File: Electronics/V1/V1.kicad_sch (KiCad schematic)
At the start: 13 parts, among them U1 ADPD144RI, U2 TCA9517ADGK, U3 XIAO-ESP32-C3, U4 TPS72218

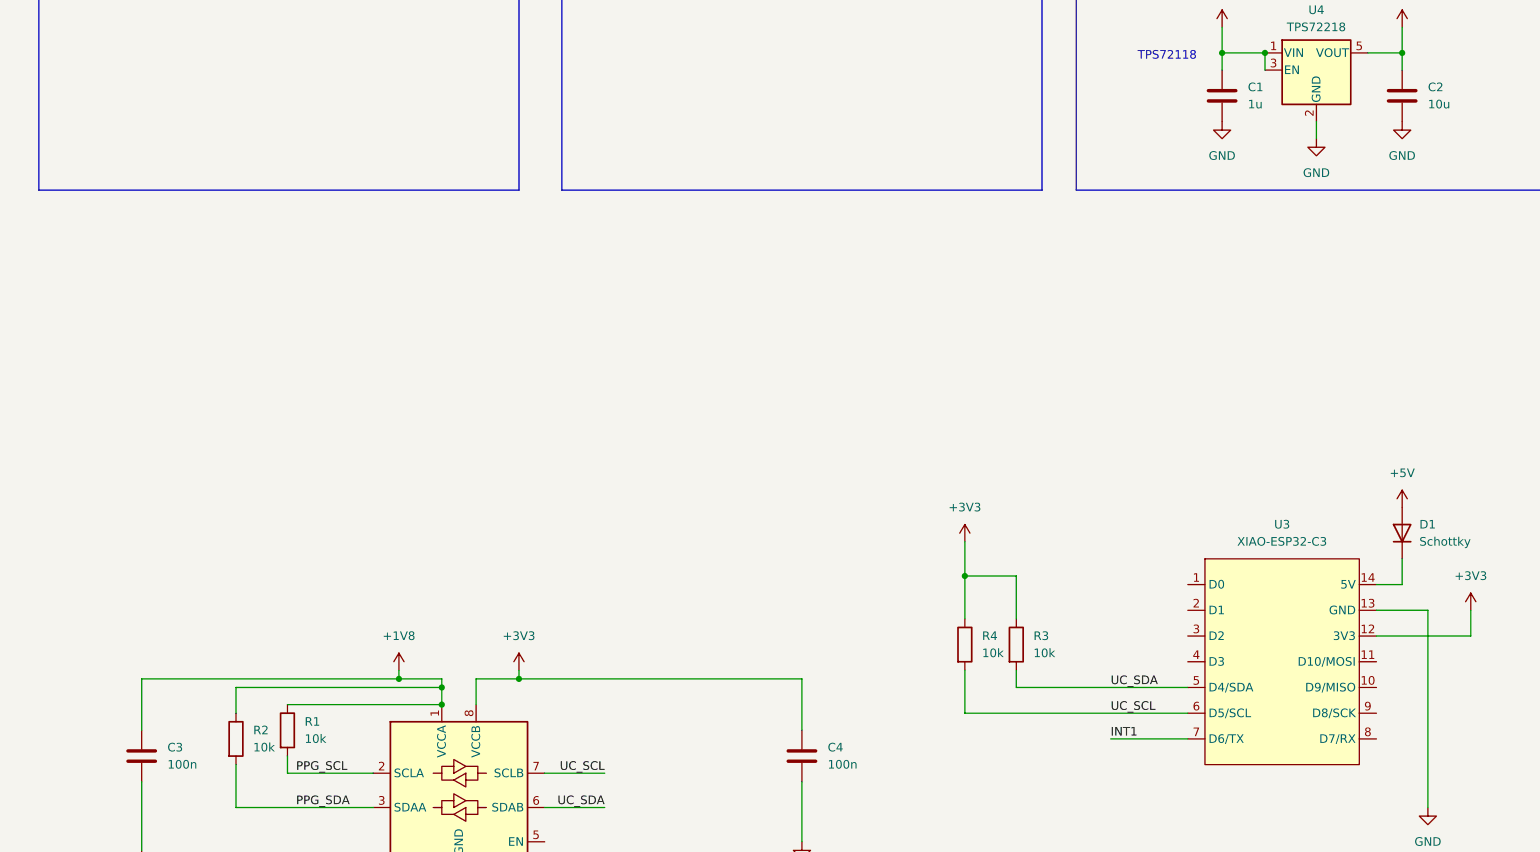
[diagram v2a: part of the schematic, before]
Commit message: Added footprint for ADPD144
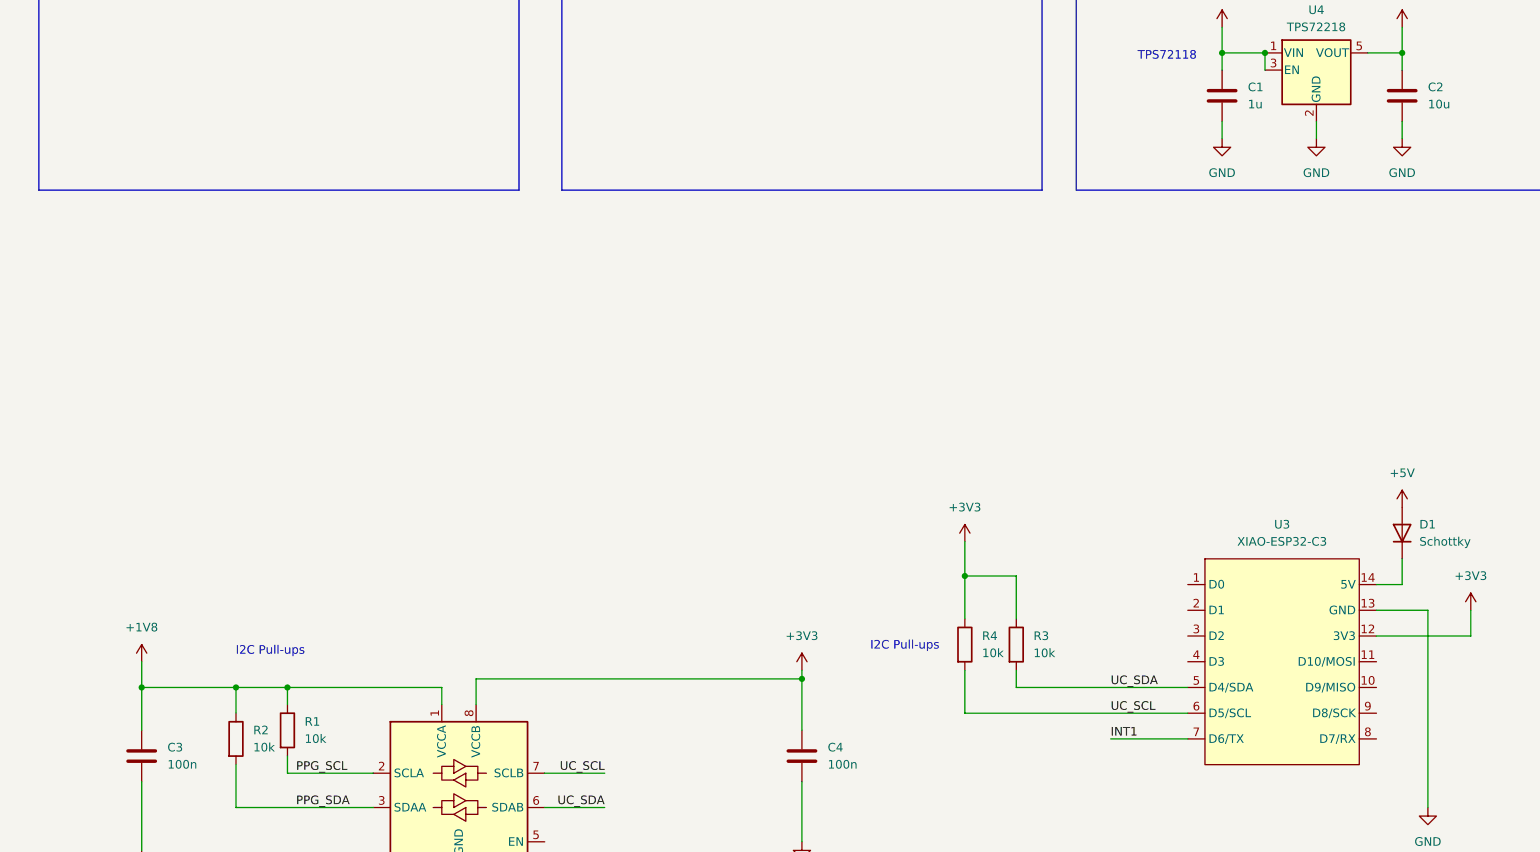
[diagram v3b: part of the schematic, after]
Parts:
- U1: footprint (none) -> CUSTOM:CE-12-2
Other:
- note added: "I2C Pull-ups"
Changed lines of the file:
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@@
+		)
+	)
+	(text "I2C Pull-ups"
+		(exclude_from_sim no)
+		(at 147.32 122.174 0)
+		(effects
+			(font
+				(size 1.27 1.27)
+			)
 		)
 	)
@@
 		)
 	)
-	(junction
-		(at 72.39 127)
-		(diameter 0)
-		(color 0 0 0 0)
-	)
-	(junction
-		(at 78.74 130.81)
-		(diameter 0)
-		(color 0 0 0 0)
+	(text "I2C Pull-ups"
+		(exclude_from_sim no)
+		(at 53.34 122.936 0)
+		(effects
+			(font
+				(size 1.27 1.27)
+			)
+		)
 	)
 	(junction
@@
 	)
 	(junction
-		(at 90.17 127)
+		(at 34.29 128.27)
 		(diameter 0)
 		(color 0 0 0 0)
 	)
 	(junction
-		(at 78.74 128.27)
+		(at 48.26 128.27)
 		(diameter 0)
 		(color 0 0 0 0)
 	)
+	(junction
+		(at 55.88 128.27)
+		(diameter 0)
+		(color 0 0 0 0)
+	)
+	(junction
+		(at 132.08 127)
+		(diameter 0)
+		(color 0 0 0 0)
+	)
 	(no_connect
 		(at 11.43 74.93)
@@
 	(wire
 		(pts
-			(xy 90.17 127) (xy 132.08 127)
-		)
-		(stroke
-			(width 0)
-			(type default)
-		)
-	)
-	(wire
-		(pts
 			(xy 194.31 34.29) (xy 200.66 34.29)
 		)
@@
 	(wire
 		(pts
+			(xy 194.31 46.99) (xy 194.31 44.45)
+		)
+		(stroke
+			(width 0)
+			(type default)
+		)
+	)
+	(wire
+		(pts
 			(xy 224.79 116.84) (xy 217.17 116.84)
 		)
@@
 	(wire
 		(pts
-			(xy 48.26 128.27) (xy 78.74 128.27)
+			(xy 48.26 128.27) (xy 55.88 128.27)
 		)
 		(stroke
@@
 	(wire
 		(pts
-			(xy 72.39 127) (xy 78.74 127)
-		)
-		(stroke
-			(width 0)
-			(type default)
-		)
-	)
-	(wire
-		(pts
 			(xy 194.31 34.29) (xy 194.31 36.83)
 		)
@@
 	(wire
 		(pts
-			(xy 72.39 125.73) (xy 72.39 127)
+			(xy 220.98 46.99) (xy 220.98 44.45)
 		)
 		(stroke
@@
 	(wire
 		(pts
+			(xy 55.88 128.27) (xy 55.88 130.81)
+		)
+		(stroke
+			(width 0)
+			(type default)
+		)
+	)
+	(wire
+		(pts
 			(xy 224.79 146.05) (xy 224.79 116.84)
 		)
@@
 	(wire
 		(pts
-			(xy 90.17 125.73) (xy 90.17 127)
+			(xy 132.08 125.73) (xy 132.08 127)
 		)
 		(stroke
@@
 	(wire
 		(pts
-			(xy 55.88 130.81) (xy 78.74 130.81)
+			(xy 55.88 128.27) (xy 78.74 128.27)
 		)
 		(stroke
@@
 	(wire
 		(pts
-			(xy 78.74 127) (xy 78.74 128.27)
-		)
-		(stroke
-			(width 0)
-			(type default)
-		)
-	)
-	(wire
-		(pts
-			(xy 34.29 134.62) (xy 34.29 127)
+			(xy 34.29 134.62) (xy 34.29 128.27)
 		)
 		(stroke
@@
 	(wire
 		(pts
-			(xy 34.29 127) (xy 72.39 127)
-		)
-		(stroke
-			(width 0)
-			(type default)
-		)
-	)
-	(wire
-		(pts
-			(xy 83.82 127) (xy 90.17 127)
+			(xy 34.29 128.27) (xy 48.26 128.27)
+		)
+		(stroke
+			(width 0)
+			(type default)
+		)
+	)
+	(wire
+		(pts
+			(xy 83.82 127) (xy 132.08 127)
 		)
 		(stroke
@@
 		(pts
 			(xy 231.14 120.65) (xy 217.17 120.65)
+		)
+		(stroke
+			(width 0)
+			(type default)
+		)
+	)
+	(wire
+		(pts
+			(xy 34.29 124.46) (xy 34.29 128.27)
 		)
 		(stroke
@@
 	(symbol
 		(lib_id "power:GND")
-		(at 220.98 44.45 0)
+		(at 220.98 46.99 0)
 		(unit 1)
 		(exclude_from_sim no)
@@
 		(fields_autoplaced yes)
 		(property "Reference" "#PWR012"
-			(at 220.98 50.8 0)
+			(at 220.98 53.34 0)
 			(effects
 				(font
@@
 		)
 		(property "Value" "GND"
-			(at 220.98 49.53 0)
+			(at 220.98 52.07 0)
 			(effects
 				(font
@@
 		)
 		(property "Footprint" ""
-			(at 220.98 44.45 0)
+			(at 220.98 46.99 0)
 			(effects
 				(font
@@
 		)
 		(property "Datasheet" ""
-			(at 220.98 44.45 0)
+			(at 220.98 46.99 0)
 			(effects
 				(font
@@
 		)
 		(property "Description" "Power symbol creates a global label with name \"GND\" , ground"
-			(at 220.98 44.45 0)
+			(at 220.98 46.99 0)
 			(effects
 				(font
@@
 	(symbol
 		(lib_id "power:+1V8")
-		(at 72.39 125.73 0)
+		(at 34.29 124.46 0)
 		(unit 1)
 		(exclude_from_sim no)
@@
 		(fields_autoplaced yes)
 		(property "Reference" "#PWR07"
-			(at 72.39 129.54 0)
+			(at 34.29 128.27 0)
 			(effects
 				(font
@@
 		)
 		(property "Value" "+1V8"
-			(at 72.39 120.65 0)
+			(at 34.29 119.38 0)
 			(effects
 				(font
@@
 		)
 		(property "Footprint" ""
-			(at 72.39 125.73 0)
+			(at 34.29 124.46 0)
 			(effects
 				(font
@@
 		)
 		(property "Datasheet" ""
-			(at 72.39 125.73 0)
+			(at 34.29 124.46 0)
 			(effects
 				(font
@@
 		)
 		(property "Description" "Power symbol creates a global label with name \"+1V8\""
-			(at 72.39 125.73 0)
+			(at 34.29 124.46 0)
 			(effects
 				(font
@@
 			)
 		)
-		(property "Footprint" ""
+		(property "Footprint" "CUSTOM:CE-12-2"
 			(at 81.28 213.36 0)
 			(effects
@@
 	(symbol
 		(lib_id "power:GND")
-		(at 194.31 44.45 0)
+		(at 194.31 46.99 0)
 		(unit 1)
 		(exclude_from_sim no)
@@
 		(fields_autoplaced yes)
 		(property "Reference" "#PWR011"
-			(at 194.31 50.8 0)
+			(at 194.31 53.34 0)
 			(effects
 				(font
@@
 		)
 		(property "Value" "GND"
-			(at 194.31 49.53 0)
+			(at 194.31 52.07 0)
 			(effects
 				(font
@@
 		)
 		(property "Footprint" ""
-			(at 194.31 44.45 0)
+			(at 194.31 46.99 0)
 			(effects
 				(font
@@
 		)
 		(property "Datasheet" ""
-			(at 194.31 44.45 0)
+			(at 194.31 46.99 0)
 			(effects
 				(font
@@
 		)
 		(property "Description" "Power symbol creates a global label with name \"GND\" , ground"
-			(at 194.31 44.45 0)
+			(at 194.31 46.99 0)
 			(effects
 				(font
@@
 	(symbol
 		(lib_id "power:+3V3")
-		(at 90.17 125.73 0)
+		(at 132.08 125.73 0)
 		(unit 1)
 		(exclude_from_sim no)
@@
 		(fields_autoplaced yes)
 		(property "Reference" "#PWR09"
-			(at 90.17 129.54 0)
+			(at 132.08 129.54 0)
 			(effects
 				(font
@@
 		)
 		(property "Value" "+3V3"
-			(at 90.17 120.65 0)
+			(at 132.08 120.65 0)
 			(effects
 				(font
@@
 		)
 		(property "Footprint" ""
-			(at 90.17 125.73 0)
+			(at 132.08 125.73 0)
 			(effects
 				(font
@@
 		)
 		(property "Datasheet" ""
-			(at 90.17 125.73 0)
+			(at 132.08 125.73 0)
 			(effects
 				(font
@@
 		)
 		(property "Description" "Power symbol creates a global label with name \"+3V3\""
-			(at 90.17 125.73 0)
-			(effects
-				(font
+			(at 132.08 125.73 0)
+			(effects
+				(font

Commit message: Added more symbols and footprints
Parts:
- added C5: 100n, Capacitor_SMD:C_0805_2012Metric_Pad1.18x1.45mm_HandSolder, symbol Device:C
- added C6: 100n, Capacitor_SMD:C_0603_1608Metric_Pad1.08x0.95mm_HandSolder, symbol Device:C
- added C7: 4u7, Capacitor_SMD:C_0603_1608Metric_Pad1.08x0.95mm_HandSolder, symbol Device:C
- added C8: 1u, Capacitor_SMD:C_0603_1608Metric_Pad1.08x0.95mm_HandSolder, symbol Device:C
- added LED1, LED2, LED3: ~, symbol Device:LED
- added PD1, PD2, PD3, PD4: D_Photo, CUSTOM:SFH2704 Photodiode, symbol Device:D_Photo
- added U5: ADPD1080, Package_CSP:LFCSP-28-1EP_5x5mm_P0.5mm_EP3.14x3.14mm, symbol CUSTOM:ADPD1080 Analog Front End
- added U6: LP2989 LDO Regulator, Package_SO:SOIC-8_3.9x4.9mm_P1.27mm, symbol CUSTOM:LP2989 LDO Regulator
- C3, C4: footprint Capacitor_SMD:C_0603_1608Metric_Pad1.08x0.95mm_HandSolder -> Capacitor_SMD:C_0805_2012Metric_Pad1.18x1.45mm_HandSolder
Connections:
- net +1V8: now also C5.1, C6.1, U5.3 (DVDD), U5.6 (AVDD)
- net GND: now also C5.2, C6.2, C7.2, C8.2, U5.26 (LGND), U5.29 (DGND), U5.4 (AGND)
- net PPG_SCL: now also U5.27 (SCL)
- net PPG_SDA: now also U5.28 (SDA)
- new net: PD4.2 (A), U5.10 (PD4)
- new net: PD3.2 (A), U5.9 (PD3)
- new net: LED1.1 (K), U5.23 (LEDX1)
- new net: LED3.1 (K), U5.25 (LEDX3)
- new net: PD2.2 (A), U5.8 (PD2)
- new net: C8.1, U5.5 (VREF)
- new net: U5.16 (NC), U5.17 (NC), U5.18 (NC), U5.19 (NC), U5.20 (NC), U5.21 (NC), U5.22 (NC)
- new net: LED2.1 (K), U5.24 (LEDX2)
- new net: PD1.2 (A), U5.7 (PD1)
- new net AFE_0: U5.1 (GPIO0)
- new net AFE_1: U5.2 (GPIO1)
- new net PD_K: PD1.1 (K), PD2.1 (K), PD3.1 (K), PD4.1 (K), U5.11 (PDC)
- new net VLED: C7.1, LED1.2 (A), LED2.2 (A), LED3.2 (A)
- no-connect marks 1 -> 5
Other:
- note added: "1.8V Reg"
- note added: "3.3V Reg"
- note added: "3.3V for VLED (N.B. Microcontroller does not put out enough current for LED) Current minimum: 500mA"
- note added: "3V - 9V"
- note added: "5V Supply for Microcontroller (N.B. use 5V as main VCC bus) 500mA ish. Vin = 3-9V ish"
- note added: "5V supply"
- note added: "Battery"
- note added: "Microcontroller"
- note removed: "3.3V for VLED (N.B. Microcontroller does not put out enough current for LED)"
- note removed: "5V Supply for Microcontroller (N.B. use 5V as main VCC bus)"
- moved on the sheet: C4

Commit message: Added level shifter for gpio, 5V reg, battery monitor and changed some footprints.
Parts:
- removed LED1, LED2, LED3: ~, symbol Device:LED
- removed U1: ADPD144RI, CUSTOM:CE-12-2, symbol CUSTOM:ADPD144RI
- added C10, C9: 100n, Capacitor_SMD:C_0805_2012Metric_Pad1.18x1.45mm_HandSolder, symbol Device:C
- added C11, C12: 10uF, symbol Device:C_Polarized
- added D2: Schottky, symbol Device:D
- added D3, D4: 3V3 LED, symbol Device:LED
- added J1: BATTERY, symbol Connector_Generic:Conn_01x02
- added J3: GPIO, Connector_PinHeader_2.54mm:PinHeader_1x08_P2.54mm_Vertical, symbol Connector_Generic:Conn_01x08
- added LED1: SFH-7016, CUSTOM:SFH-7016 Multi Chip LED, symbol CUSTOM:SFH-7016
- added R10, R9: 330, symbol Device:R
- added R5: changeme, symbol Device:R
- added R6: 0R, symbol Device:R
- added R7: 15k, symbol Device:R
- added R8: 12k, symbol Device:R
- added SW1: SW_SPST, symbol Switch:SW_SPST
- added U7: TXB0102DCU, Package_SO:VSSOP-8_2.3x2mm_P0.5mm, symbol Logic_LevelTranslator:TXB0102DCU
- added U8: MAX603, Package_DIP:DIP-8_W10.16mm_LongPads, symbol Regulator_Linear:MAX603
- PD1, PD2, PD3, PD4: value D_Photo -> SFH2200; footprint CUSTOM:SFH2704 Photodiode -> CUSTOM:TOPLED D5140
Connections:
- net +1V8: now also C9.1, R6.1, U7.3 (VCCA)
- net +3V3: now also C10.1, J3.3 (Pin_3), R9.1, U7.7 (VCCB)
- net +5V: now also C12.1, J3.1 (Pin_1), U8.8 (OUT)
- net AFE_0: now also U7.5 (A1)
- net AFE_1: now also U7.4 (A2)
- net GND: now also C10.2, C11.2, C12.2, C9.2, D3.1 (K), D4.1 (K), J3.2 (Pin_2), J3.4 (Pin_4), R5.2, R8.2, SW1.2 (B), U7.2 (GND), U8.2 (GND), U8.3 (GND), U8.5 (SET), U8.6 (GND), U8.7 (GND)
- net VLED: now also LED1.2 (A), LED1.2 (A), LED1.2 (A), LED1.5 (A), LED1.5 (A), LED1.5 (A)
- net at U5.23 (LEDX1): now also LED1.1 (KIR)
- net at U5.25 (LEDX3): now also LED1.4 (KRED)
- net at U5.24 (LEDX2): now also LED1.3 (KGREEN)
- net UC_D0: now reaches U3.1 (D0)
- net UC_D0: now also U7.8 (B1)
- net UC_D9: now reaches U3.10 (D9/MISO)
- net UC_D9: now also J3.6 (Pin_6)
- net UC_D10: now reaches U3.11 (D10/MOSI)
- net UC_D10: now also J3.5 (Pin_5)
- net UC_D1: now reaches U3.2 (D1)
- net UC_D1: now also U7.1 (B2)
- net BAT_SENSE: now reaches U3.3 (D2)
- net BAT_SENSE: now also R7.2, R8.1
- net I2C_EN: now reaches U3.4 (D3)
- net I2C_EN: now also U2.5 (EN)
- net UC_D7: now reaches U3.8 (D7/RX)
- net UC_D7: now also J3.8 (Pin_8)
- net UC_D8: now reaches U3.9 (D8/SCK)
- net UC_D8: now also J3.7 (Pin_7)
- net INT1 renamed UC_D6
- net UC_D6: now also R10.1
- new net: D4.2 (A), R10.2
- new net: R5.1, R6.2, U7.6 (OE)
- new net: D3.2 (A), R9.2
- new net BAT+: D2.2 (A), J1.1 (Pin_1)
- new net BAT-: J1.2 (Pin_2), SW1.1 (A)
- new net VBAT: C11.1, D2.1 (K), R7.1, U8.1 (IN), U8.4 (~{OFF})
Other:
- note added: "0.45 Voltage divider for battery voltage sensing."
- note added: "Choose a pull down"
- note added: "Define VLED"
- note added: "Do i need this?"
- note added: "Green"
- note added: "Infrared"
- note added: "Red"
- note added: "Verfiy pins"
- note added: "gpio Level shifter required for communication between OFE (1.8V) and Microcontroller (3.3v)"
- note added: "i2c Level shifter required for communication between OFE (1.8V) and Microcontroller (3.3v)"
- note removed: "Level shifter required for communication between OFE (1.8V) and Microcontroller (3.3v)"
- note removed: "TODO: Add I2C pull-up resistors"
- moved on the sheet: C1, C2, C3, C4, C5, C6, C7, C8, PD1, R1, R2, U2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

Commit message: Added Seeed Studio footprint
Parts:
- removed U6: LP2989 LDO Regulator, Package_SO:SOIC-8_3.9x4.9mm_P1.27mm, symbol CUSTOM:LP2989 LDO Regulator
- C10, C3, C4, C5, C9: footprint Capacitor_SMD:C_0805_2012Metric_Pad1.18x1.45mm_HandSolder -> Capacitor_SMD:C_0603_1608Metric_Pad1.08x0.95mm_HandSolder
- C11, C12: footprint (none) -> Capacitor_SMD:C_1210_3225Metric_Pad1.33x2.70mm_HandSolder
- D1, D2: value Schottky -> B130LAW-7-F; footprint (none) -> Diode_SMD:D_SOD-123
- D3, D4: footprint (none) -> LED_SMD:LED_0805_2012Metric_Pad1.15x1.40mm_HandSolder
- J1: footprint (none) -> TerminalBlock:TerminalBlock_bornier-2_P5.08mm
- R1, R10, R2, R3, R4, R5, R6, R7, R8, R9: footprint (none) -> Resistor_SMD:R_0603_1608Metric_Pad0.98x0.95mm_HandSolder
- U3: footprint (none) -> CUSTOM:Seeed Studio XIAO ESP32-C3
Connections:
- no-connect marks 5 -> 4
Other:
- note removed: "1.8V Reg"
- note removed: "3.3V Reg"
- note removed: "3V - 9V"
- note removed: "5V supply"
- note removed: "Battery"
- note removed: "Microcontroller"
- moved on the sheet: D2, D3, J1, R7, R8, R9, SW1

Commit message: Minor fixes
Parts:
- D4: value 3V3 LED -> CTRL LED
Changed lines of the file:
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@@
 			)
 		)
-		(property "Value" "3V3 LED"
+		(property "Value" "CTRL LED"
 			(at 181.61 155.2574 90)
 			(effects

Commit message: Some unfinished PCB changes
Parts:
- removed D2: B130LAW-7-F, Diode_SMD:D_SOD-123, symbol Device:D
- removed SW1: SW_SPST, symbol Switch:SW_SPST
- removed U8: MAX603, Package_DIP:DIP-8_W10.16mm_LongPads, symbol Regulator_Linear:MAX603
- added H1, H2: MountingHole, MountingHole:MountingHole_3.2mm_M3, symbol Mechanical:MountingHole
- added Q1, Q3: PMV41XPAR, Package_TO_SOT_SMD:SOT-23, symbol Transistor_FET:AO3401A
- added R11: 10k, Resistor_SMD:R_0603_1608Metric_Pad0.98x0.95mm_HandSolder, symbol Device:R
- added R12: 0R, Resistor_SMD:R_0603_1608Metric_Pad0.98x0.95mm_HandSolder, symbol Device:R
- added SW1: PVA1 EE H1 3.5N V2, Button_Switch_THT:SW_Push_2P1T_Toggle_CK_PVA1xxH1xxxxxxV2, symbol Switch:SW_DPST
- added U1: TPS7A4533, Package_TO_SOT_SMD:SOT-223-6, symbol CUSTOM:TPS7A45xx
- C11, C12: footprint Capacitor_SMD:C_1210_3225Metric_Pad1.33x2.70mm_HandSolder -> Capacitor_SMD:C_0805_2012Metric_Pad1.18x1.45mm_HandSolder
- J1: value BATTERY -> BA9VPC; footprint TerminalBlock:TerminalBlock_bornier-2_P5.08mm -> Battery:BatteryHolder_MPD_BA9VPC_1xPP3
- R7: value 15k -> 20k
- R8: value 12k -> 10k
- U3: symbol CUSTOM:Seeed_XIAO_ESP32 -> CUSTOM:Seeed_XIAO_ESP32 Development Board
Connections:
- net BAT- is gone; now on net GND: J1.2 (Pin_2)
- net VLED is gone; now on net +3V3: C7.1, LED1.2 (A), LED1.2 (A), LED1.2 (A), LED1.5 (A), LED1.5 (A), LED1.5 (A)
- net +3V3: now also C1.1, C12.1, J3.1 (Pin_1), J3.2 (Pin_2), U4.1 (VIN), U4.3 (EN), Q1.3 (D), U1.4 (OUT), U1.5 (ADJ); no longer J3.3 (Pin_3), R9.1, U3.12 (3V3)
- net BAT+: now also Q3.3 (D), R11.1, R12.1
- net GND: now also J3.3 (Pin_3), SW1.2, SW1.4, U1.3 (GND), U1.6 (GND); no longer J3.2 (Pin_2)
- net VBAT: now also D1.1 (K), U1.1 (~{SHDN}), U1.2 (IN)
- net VUSB: now reaches U3.14 (5V)
- net VUSB: now also Q1.1 (G); no longer D1.1 (K)
- removed net +5V: C1.1, C12.1, D1.2 (A), J3.1 (Pin_1), U4.1 (VIN), U4.3 (EN)
- new net: D1.2 (A), Q3.2 (S), R12.2
- new net: Q3.1 (G), R11.2, SW1.1, SW1.3
- new net: Q1.2 (S), R9.1, U3.12 (3V3)
- now unconnected: U5.16 (NC), U5.17 (NC), U5.18 (NC), U5.19 (NC), U5.20 (NC), U5.21 (NC), U5.22 (NC)
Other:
- note added: "Maximum voltage at cathode of LED is 3.6V Quick check: 3.3V - VLED (~2.5V) = 0.8V < 3.6V"
- note added: "Use PP3 9V battery: VBAT = 7-9.6V"
- note added: "When USB connected, 3.3V input disabled to the ESP32-C3"
- note removed: "0.45 Voltage divider for battery voltage sensing."
- note removed: "5V Supply for Microcontroller (N.B. use 5V as main VCC bus) 500mA ish. Vin = 3-9V ish"
- note removed: "Define VLED"
- note removed: "Do i need this?"
- note removed: "Verfiy pins"
- moved on the sheet: C1, C11, C12, C2, C5, C6, C7, C8, D3, D4, J1, J3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
